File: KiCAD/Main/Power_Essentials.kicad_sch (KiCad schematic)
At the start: 25 parts, among them J1 Micro_SD_Card_Det2, J2 Screw_Terminal_01x09, J3 Screw_Terminal_01x09, J4 USB_C_Receptacle_USB2.0_16P, Q1 AO3400A, Q2 AO3400A, Q3 AO3400A, U1 LM2596S-3.3, U2 TPS2121RUXR

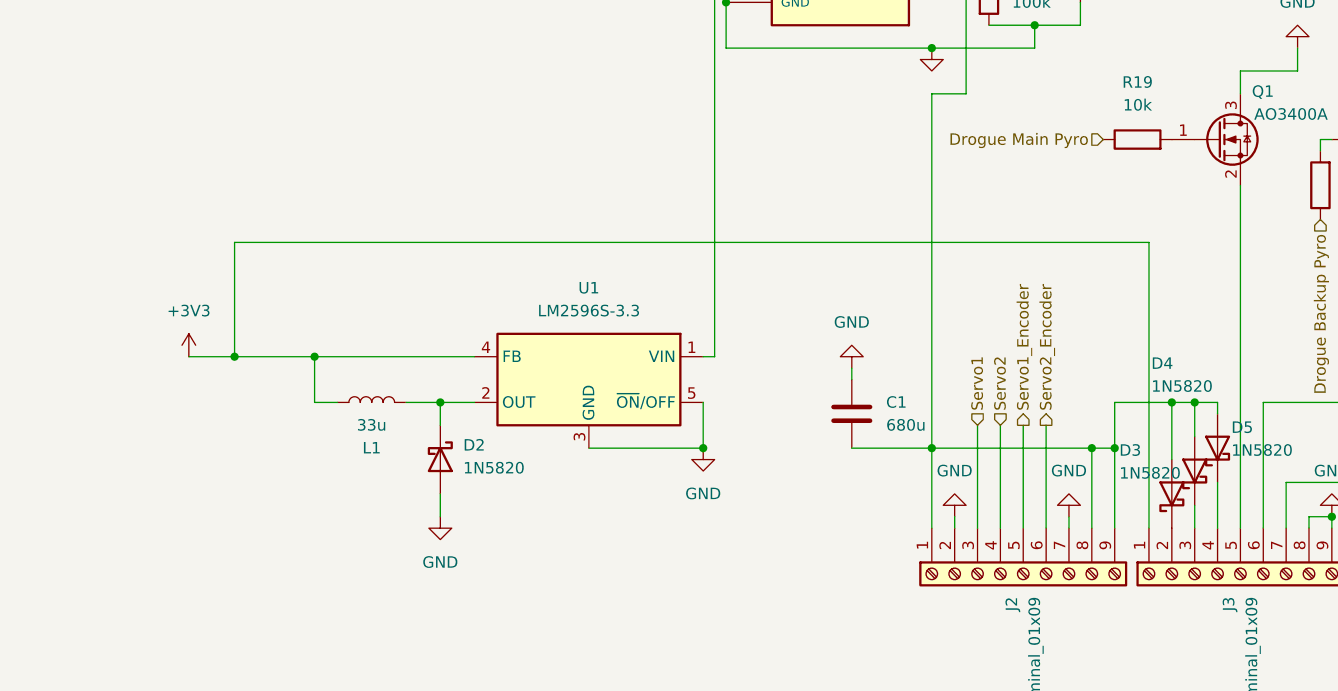
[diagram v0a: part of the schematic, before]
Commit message: Update RF sys and footprints
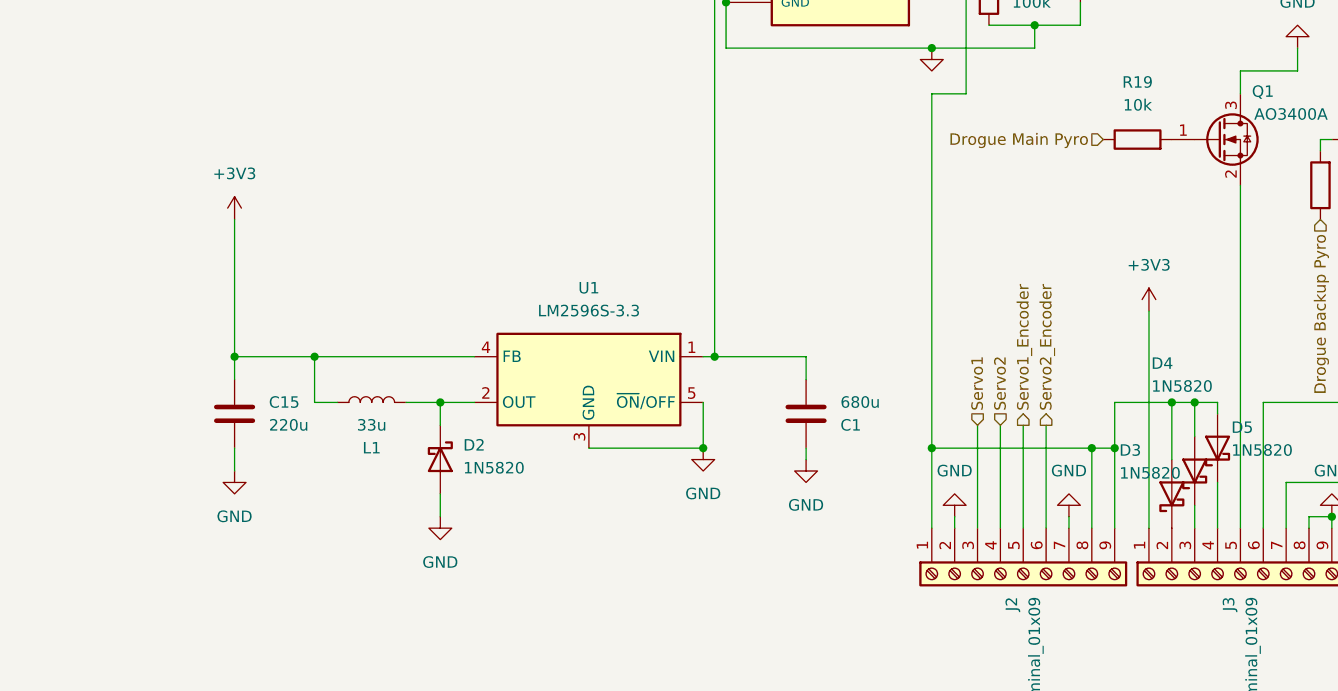
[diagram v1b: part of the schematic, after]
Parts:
- added C15: 220u, Capacitor_SMD:C_0603_1608Metric, symbol Device:C
- C1, C2: footprint (none) -> Capacitor_SMD:C_0603_1608Metric
- J1: footprint (none) -> Connector_Card:microSD_HC_Hirose_DM3AT-SF-PEJM5
- J2, J3: footprint (none) -> Connector_Phoenix_MSTB:PhoenixContact_MSTBVA_2,5_9-G_1x09_P5.00mm_Vertical
- J4: footprint (none) -> Connector_USB:USB_C_Receptacle_HRO_TYPE-C-31-M-12
- L1: footprint (none) -> Inductor_SMD:L_0603_1608Metric
- R19, R20, R21, R3, R5, R6, R7, R8: footprint (none) -> Resistor_SMD:R_0603_1608Metric
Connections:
- net +3V3: now also C15.1
- net GND: now also C15.2
- net at U1.1 (VIN), U2.1 (OUT), U2.1_1 (OUT)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: now also C1.2
- net at D3.2 (A), D4.2 (A), D5.2 (A)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: no longer C1.2
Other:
- moved on the sheet: C1
